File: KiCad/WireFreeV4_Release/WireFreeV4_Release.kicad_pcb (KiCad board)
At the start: 6 copper layers, 14.3 x 15.4 mm, 44 parts, among them J1 Conn_01x05, J10 Conn_01x01, J11 Conn_01x01, J12 Conn_01x01, J13 Conn_01x01, J14 Conn_01x01, J15 Conn_01x01, J2 Conn_01x28, J3 Conn_01x01, J4 Conn_01x01, J8 0475710001, U1 TPS62402-Q1, U2 MAX13030EETE+, U3 ATSAME70N21A-CN, U4 TSOP57438TT1, Y1 ABM8G-12.000MHZ-4Y-T3

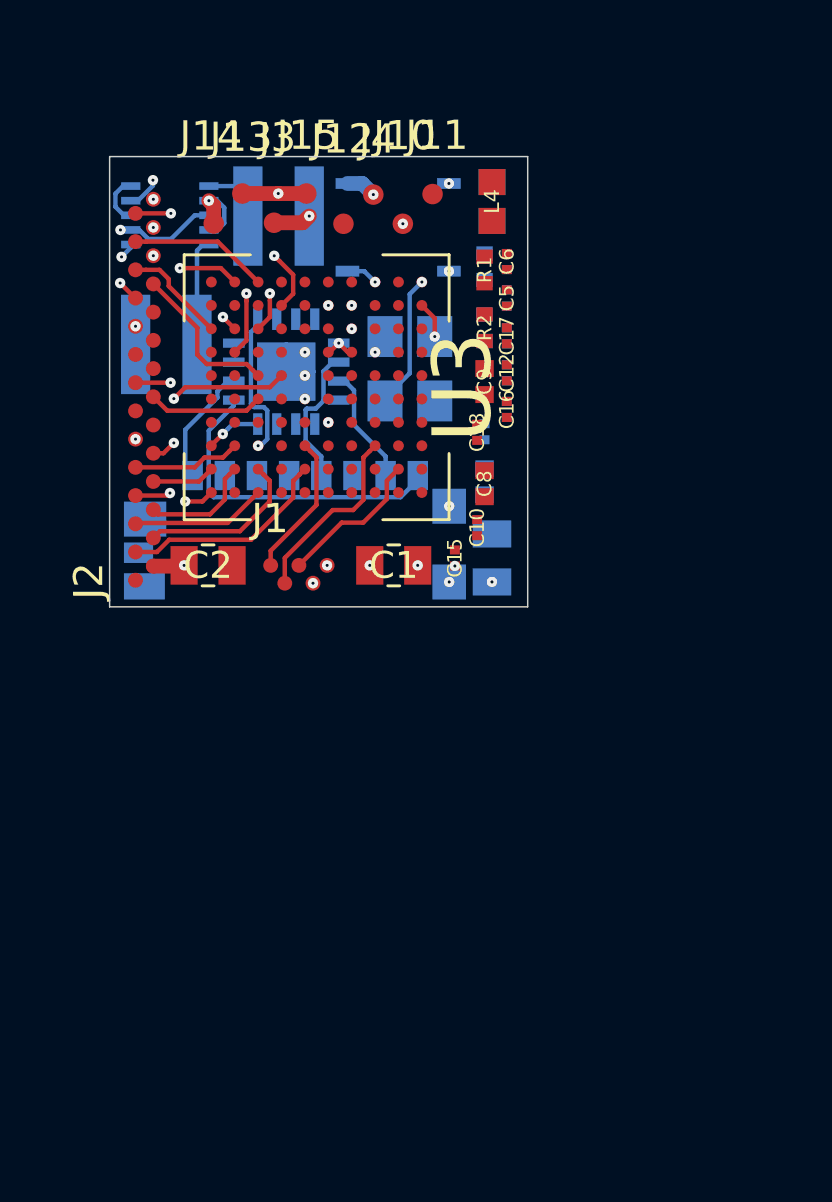
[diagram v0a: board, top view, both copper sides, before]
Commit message: Wire-free KiCAD Updates
1. Almost all lines are connected except some power lines and a few signal lines that lead to capacitors

2. About ten capacitors left to find their spot on the board

3. Rearranged the capacitor locations and connector pad locations to bring power converter SMDs closer to the IU.
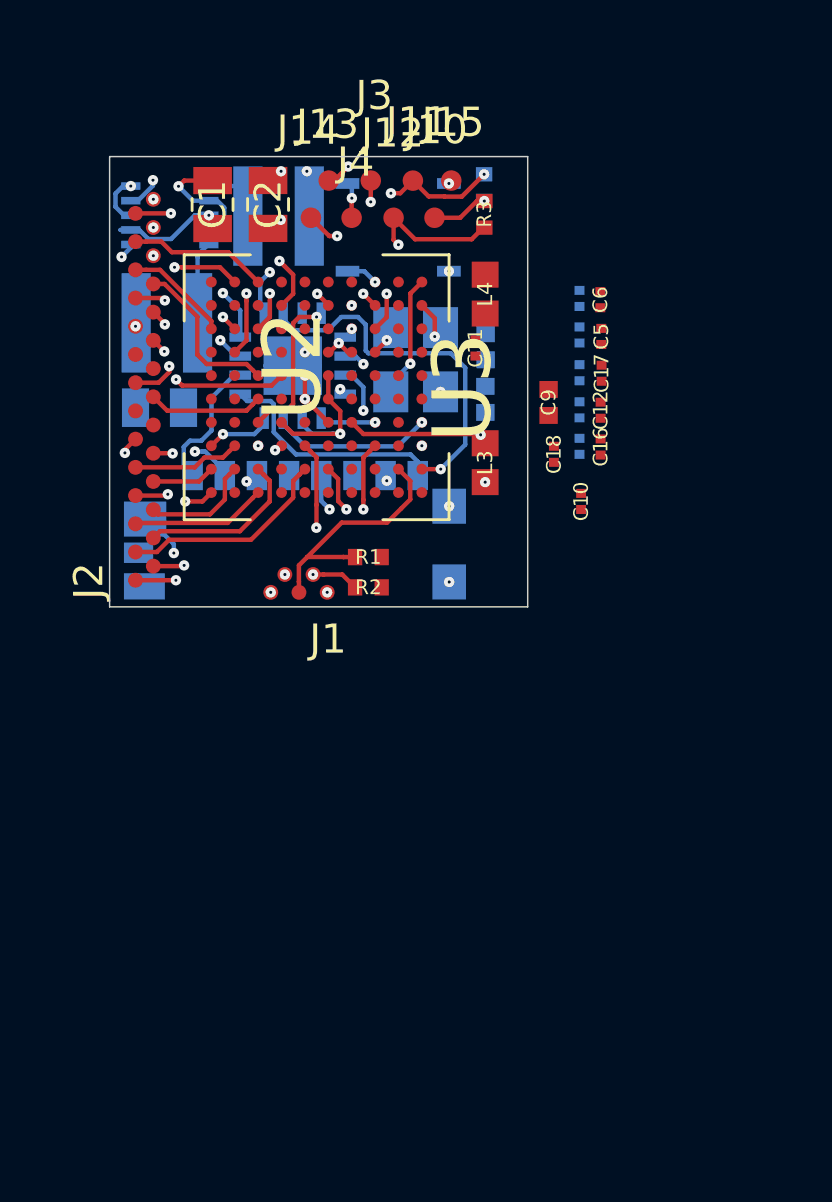
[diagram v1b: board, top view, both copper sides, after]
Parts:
- C11, L3, R3: moved to F.Cu
- C15, C8: moved to B.Cu
- moved C1 13.8 mm to (119.2, 72.2), turned to 270 degrees
- moved C2 12.5 mm to (121.1, 72.2), turned to 270 degrees
- moved C3 12.5 mm to (117.4, 79.2), turned to 0 degrees
- moved R1 10.6 mm to (124.6, 84.3), turned to 0 degrees
- moved R2 9.73 mm to (124.6, 85.3), turned to 0 degrees
- moved L3 8.94 mm to (128.5, 81.1), turned to 90 degrees
- moved J15 4.98 mm to (127.4, 71.4)
- moved C7 4.62 mm to (128.6, 77.1), turned to 270 degrees
- moved C15 4.03 mm to (128.4, 80.4)
- moved R3 3.88 mm to (128.5, 72.6)
- moved C10 3.67 mm to (131.8, 82.4)
- moved J3 3.61 mm to (124.6, 71.4)
- moved C5 3.49 mm to (132.5, 76.8)
- moved C17 3.49 mm to (132.5, 78.0)
- moved C16 3.46 mm to (132.5, 80.5)
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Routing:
- net /Connectors/SWDCLK: track 0.00 -> 16.6 mm, vias 0 -> 2
- net /Connectors/SWDIO: track 0.00 -> 14.6 mm, vias 0 -> 3
- net /MCU/SDCardCMDA: track 0.00 -> 12.5 mm, vias 0 -> 1
- net /SD Card/DAT3: track 0.00 -> 9.30 mm, vias 0 -> 2
- net Net-(J8-PadP3): track 0.00 -> 8.97 mm, vias 0 -> 2
- net +1V8: track 3.52 -> 11.4 mm, vias 4 -> 8
- net Earth: track 8.63 -> 14.8 mm, vias 17 -> 19
- net /MCU/SD1: track 0.00 -> 5.60 mm, vias 0 -> 1
- net /MCU/SDCardCLKA: track 0.00 -> 5.32 mm, vias 0 -> 1
- net /MCU/VDDPLL: track 0.00 -> 4.86 mm, vias 0 -> 1
- net /Connectors/SDA: track 5.14 -> 8.51 mm
- net /SD Card/DAT1: track 11.1 -> 8.06 mm
- net +BATT: track 4.36 -> 7.40 mm, vias 2 -> 4
- net /MCU/SD3: track 5.03 -> 7.97 mm, vias 1 -> 2
- net Net-(J8-PadP5): track 4.87 -> 7.45 mm, vias 0 -> 2
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
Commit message: Update Release Board KiCAD
1. Rotate the micro SD card mount
2. Place all capacitors
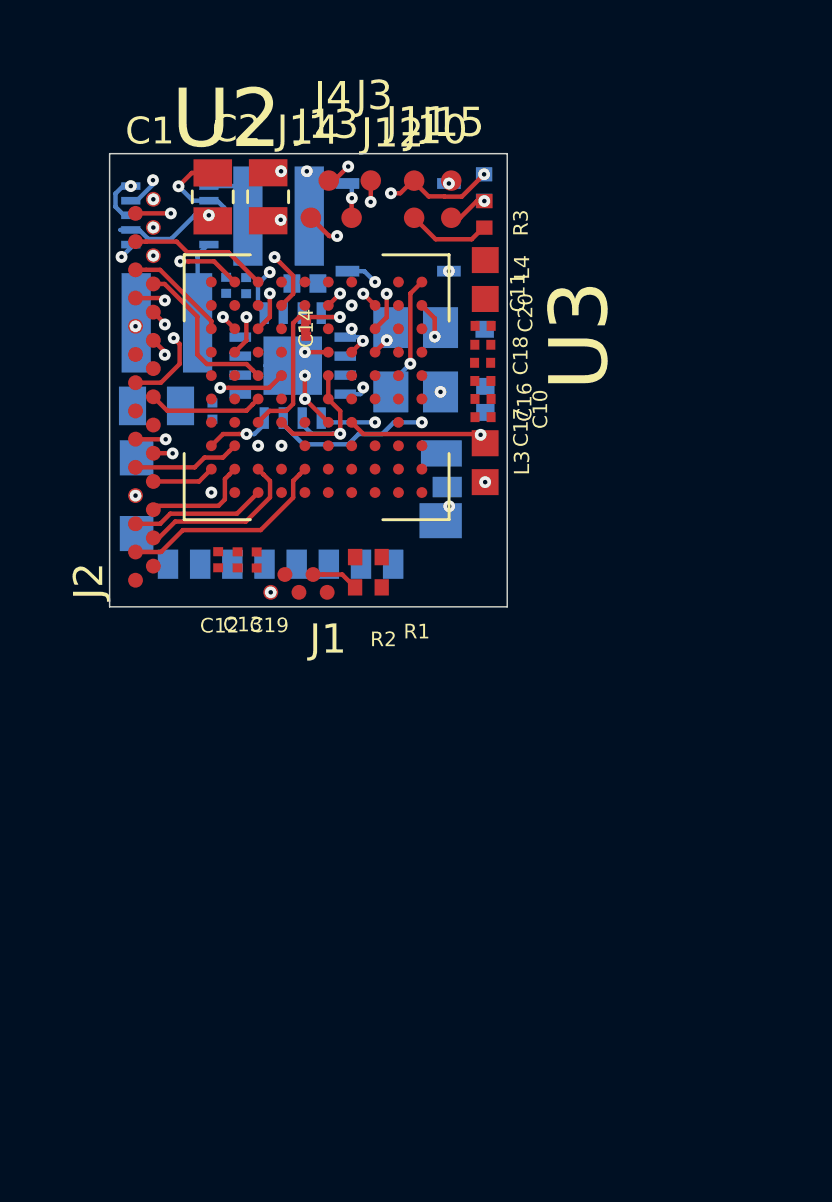
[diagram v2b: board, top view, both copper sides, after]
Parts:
- C13, C14, C19, C20: moved to F.Cu
- C5, C6, C9: moved to B.Cu
- moved C12 14.0 mm to (119.4, 84.4)
- moved C13 14.0 mm to (120.1, 84.4), turned to 90 degrees
- moved C6 13.8 mm to (119.2, 79.3)
- moved C5 13.0 mm to (119.7, 75.0), turned to 270 degrees
- moved C19 12.8 mm to (120.7, 84.4), turned to 90 degrees
- moved C4 11.4 mm to (120.4, 75.0)
- moved C14 9.76 mm to (122.4, 76.5), turned to 90 degrees
- moved C9 9.27 mm to (122.4, 74.9), turned to 180 degrees
- moved C16 4.96 mm to (128.5, 77.7), turned to 0 degrees
- moved C10 4.85 mm to (128.5, 78.9), turned to 180 degrees
- moved C18 4.47 mm to (128.5, 77.0), turned to 0 degrees
- moved C17 4.32 mm to (128.5, 79.5), turned to 180 degrees
- moved C20 3.99 mm to (128.5, 78.3), turned to 0 degrees
- moved J8 3.15 mm to (121.5, 84.5), turned to 0 degrees
- moved C7 1.04 mm to (128.5, 76.1), turned to 90 degrees
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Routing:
- net /Connectors/SWDCLK: track 16.6 -> 2.87 mm, vias 2 -> 0
- net /MCU/SDCardCMDA: track 12.5 -> 0.00 mm, vias 1 -> 0
- net /SD Card/DAT3: track 9.30 -> 0.00 mm, vias 2 -> 0
- net Net-(J8-PadP3): track 8.97 -> 0.00 mm, vias 2 -> 0
- net /Connectors/SDA: track 8.51 -> 0.00 mm
- net /SD Card/DAT1: track 8.06 -> 0.00 mm
- net Net-(J8-PadP5): track 7.45 -> 0.00 mm, vias 2 -> 0
- net /Connectors/LED_ENT: track 6.10 -> 0.00 mm, vias 2 -> 0
- net /Connectors/SCL: track 7.13 -> 1.62 mm, vias 2 -> 0
- net /SD Card/DAT2: track 5.14 -> 0.00 mm
- net /SD Card/DAT0: track 4.52 -> 0.00 mm, vias 2 -> 0
- net Earth: track 14.8 -> 12.7 mm, vias 19 -> 14
- net /CMOS Imaging Sensor Connectors/CLK_OUT: track 10.3 -> 8.55 mm
- net +1V8: track 11.4 -> 9.78 mm, vias 8 -> 7
- net /MCU/SDCardCLKA: track 5.32 -> 6.61 mm
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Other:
- board size 14.3 x 15.4 mm -> 13.6 x 15.5 mm

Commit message: Update WireFreeV4_Release.kicad_pcb
Last update before an overhaul:

1. Change SWD to Pogo pins
2. Rearrange the capacitors and pins
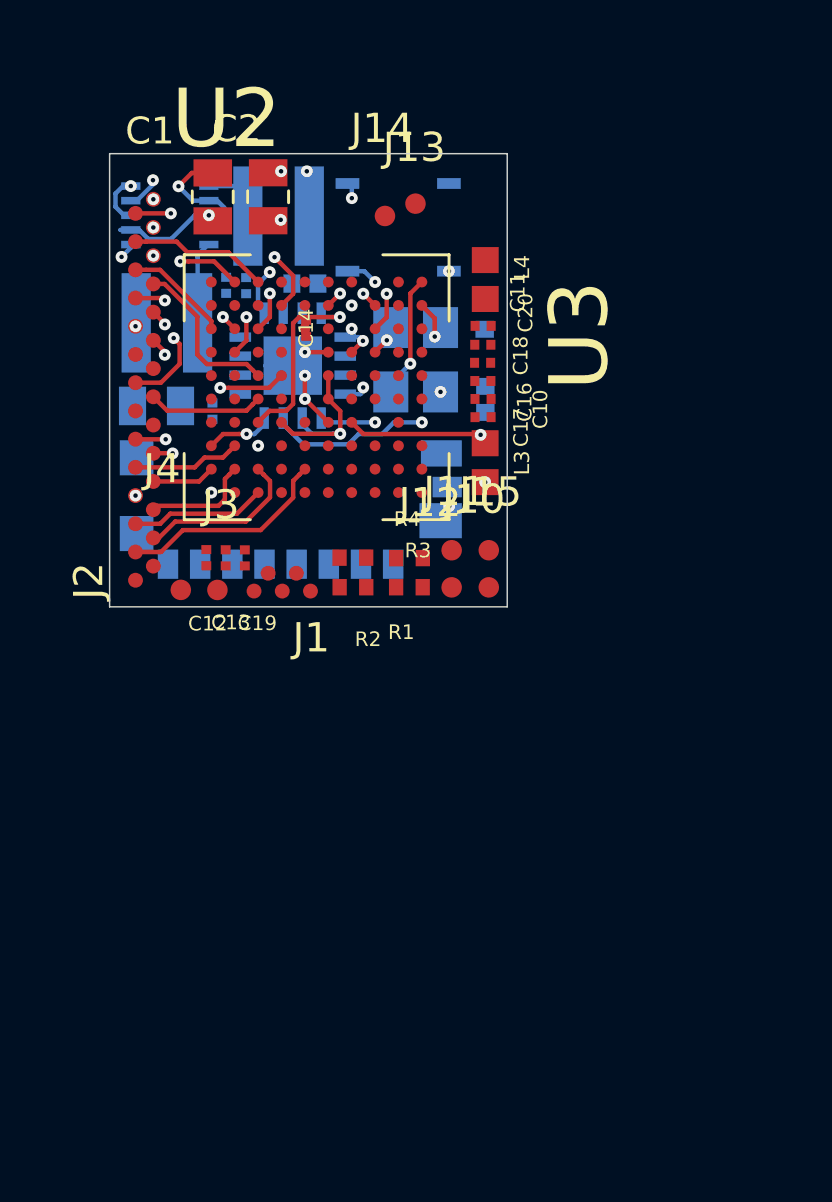
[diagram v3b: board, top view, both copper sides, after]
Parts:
- R4: moved to F.Cu
- moved J3 15.0 mm to (119.4, 85.4)
- moved J4 14.0 mm to (118.1, 85.4)
- moved R3 13.0 mm to (126.0, 85.3), turned to 0 degrees
- moved R4 12.9 mm to (126.0, 84.3), turned to 0 degrees
- moved J12 12.7 mm to (126.7, 85.3)
- moved J11 12.7 mm to (127.4, 84.1)
- moved J15 12.7 mm to (128.7, 84.1)
- moved J10 12.7 mm to (128.1, 85.3)
- moved J13 3.07 mm to (126.2, 72.2)
- moved J14 2.53 mm to (125.1, 72.6)
- moved J1 0.57 mm to (122.6, 85.5)
- moved R1 0.53 mm to (124.0, 84.3)
- moved R2 0.53 mm to (124.0, 85.3)
- moved C19 0.41 mm to (120.3, 84.3)
- moved C12 0.41 mm to (119.0, 84.3)
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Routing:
- net /Connectors/SWDIO: track 14.1 -> 0.00 mm, vias 3 -> 0
- net /Connectors/SWDCLK: track 2.87 -> 0.00 mm
- net +1V8: track 9.78 -> 7.68 mm, vias 7 -> 5
- net /Connectors/SCL: track 1.62 -> 0.00 mm
- net +BATT: track 7.63 -> 6.48 mm, vias 4 -> 3
- net Earth: track 12.7 -> 11.9 mm, vias 14 -> 12
- net +3V3: track 2.58 -> 1.92 mm, vias 5 -> 4

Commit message: PCB Layout Overhaul
1. Places the microSD and MCU on the same side

2. Sketches the outline with the components placed

3. No traces or vias yet
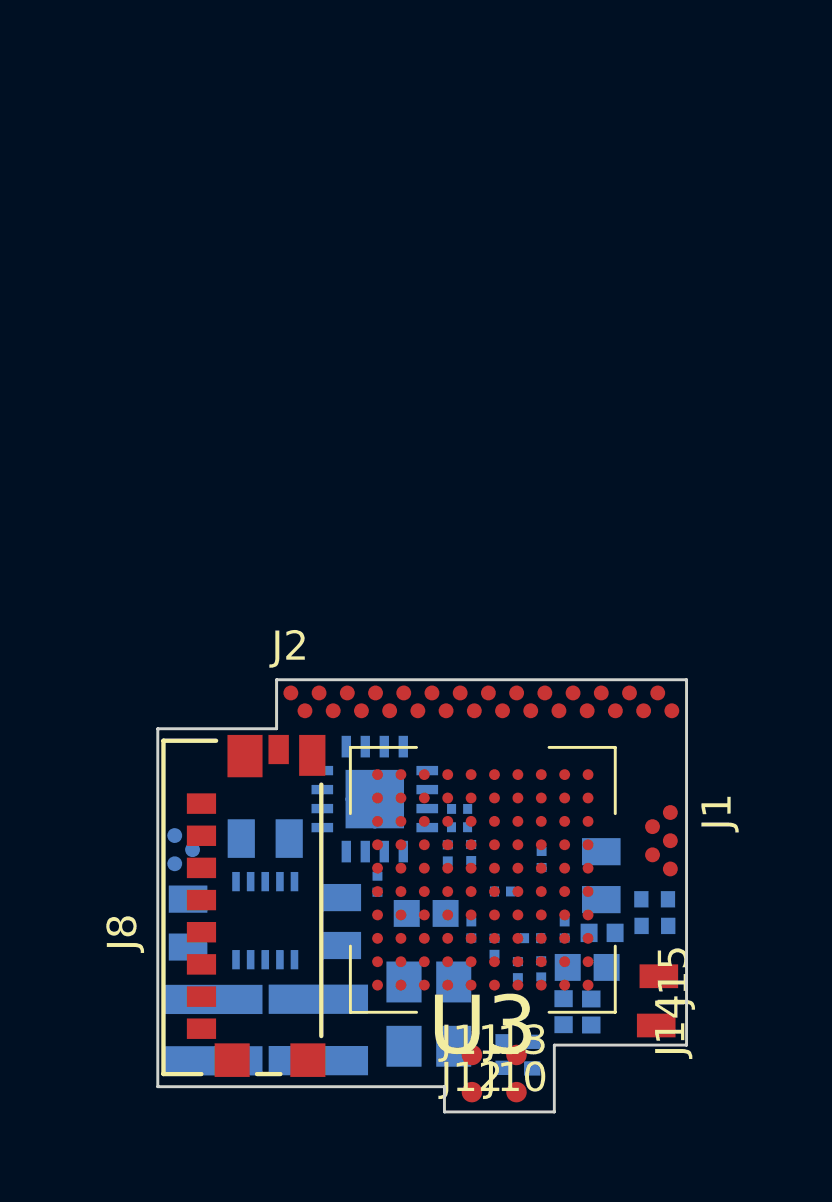
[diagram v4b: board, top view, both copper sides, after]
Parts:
- removed J4: Conn_01x01, .Connector:Conn_1x1_700_Circular_Pad
- removed U4: TSOP57438TT1, .Package_SON:SON_4_P300_395X395X90L55X35L
- added C21: C_Small, .Capacitor:C_0805_2012Metric_L, B.Cu at (132.5, 95.2)
- C1, C10, C11, C12, C13, C14, C16, C17, C18, C19, C2, C20, L3, L4, R1, R2, R3, R4: moved to B.Cu
- J14, J15: footprint .Connector:Conn_1x1_700_Circular_Pad -> .Connector:Conn_1x1_250x750_Pad
- J3: value Conn_01x01 -> Conn_01x03; footprint .Connector:Conn_1x1_700_Circular_Pad -> .Connector:B2B_Flex_03_Dual_Row_38milx24mil_Pad_20mil_copy; moved to B.Cu
- J8: moved to F.Cu
- moved J13 29.3 mm to (129.6, 101.3), turned to 180 degrees
- moved J14 29.2 mm to (134.4, 100.3), turned to 90 degrees
- moved L1 27.9 mm to (119.2, 100.5), turned to 270 degrees
- moved C2 25.0 mm to (118.4, 96.8), turned to 90 degrees
- moved L2 24.7 mm to (122.8, 100.5), turned to 270 degrees
- moved C9 24.4 mm to (132.5, 97.2), turned to 0 degrees
- moved U1 24.3 mm to (121.0, 96.7), turned to 180 degrees
- moved C7 23.9 mm to (131.2, 99.8), turned to 270 degrees
- moved L4 23.8 mm to (132.0, 98.3), turned to 0 degrees
- moved Y1 22.4 mm to (126.6, 99.9), turned to 270 degrees
- moved C11 22.1 mm to (130.5, 98.4), turned to 270 degrees
- moved C1 22.0 mm to (121.0, 93.9), turned to 0 degrees
- moved C18 21.4 mm to (129.7, 98.4), turned to 270 degrees
- moved C8 21.3 mm to (132.2, 99.9)
- moved C4 21.0 mm to (124.9, 95.5)
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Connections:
- J3 pad 1: +1V8 -> Earth
- U3 pad C1: /MCU/IR_Receiver -> /Connectors/IR_Receiver
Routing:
- net Earth: track 11.9 -> 0.00 mm, vias 12 -> 0
- net /CMOS Imaging Sensor Connectors/CLK_OUT: track 8.55 -> 0.00 mm, vias 2 -> 0
- net /MCU/SD3: track 8.12 -> 0.00 mm, vias 2 -> 0
- net /CMOS Imaging Sensor Connectors/RESET_N: track 7.90 -> 0.00 mm, vias 2 -> 0
- net +1V8: track 7.68 -> 0.00 mm, vias 5 -> 0
- net /CMOS Imaging Sensor Connectors/LINE_VALID: track 7.62 -> 0.00 mm, vias 2 -> 0
- net /CMOS Imaging Sensor Connectors/Status_LED: track 7.50 -> 0.00 mm, vias 2 -> 0
- net /CMOS Imaging Sensor Connectors/img_d0: track 7.30 -> 0.00 mm
- net /CMOS Imaging Sensor Connectors/SCK: track 7.19 -> 0.00 mm, vias 2 -> 0
- net /CMOS Imaging Sensor Connectors/SS_N: track 6.69 -> 0.00 mm, vias 2 -> 0
- net /MCU/SDCardCLKA: track 6.61 -> 0.00 mm, vias 1 -> 0
- net +BATT: track 6.48 -> 0.00 mm, vias 3 -> 0
- net /CMOS Imaging Sensor Connectors/MONITOR0: track 6.46 -> 0.00 mm, vias 2 -> 0
- net /CMOS Imaging Sensor Connectors/img_d7: track 5.85 -> 0.00 mm, vias 2 -> 0
- net /CMOS Imaging Sensor Connectors/img_d2: track 5.70 -> 0.00 mm
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- removed copper zone on In1.Cu, net Earth
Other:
- board size 13.6 x 15.5 mm -> 18.1 x 14.8 mm

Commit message: Rearrange Release Board
1. 28-flexPC pad changed to 25-pads by eliminating the vBatt, and the I2C's

2. Dimensions: 18.92mm x 12.09mm
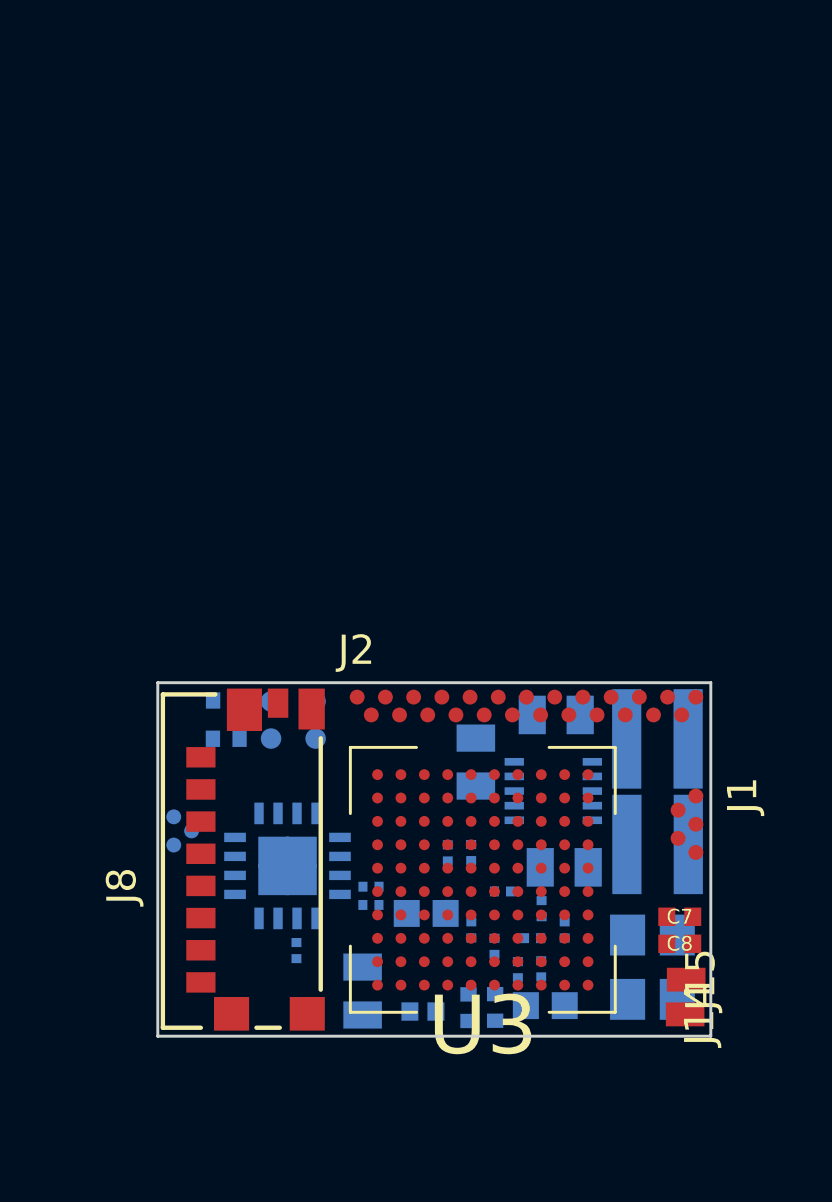
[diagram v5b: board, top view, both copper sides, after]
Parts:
- C7, C8: moved to F.Cu
- J10, J11, J12, J13: moved to B.Cu
- J2: value Conn_01x28 -> Conn_01x25; footprint .Connector:B2B_Flex_28_Dual_Row_38milx24mil_Pad_20mil -> .Connector:B2B_Flex_25_Dual_Row_38milx24mil_Pad_20mil
- moved L1 16.5 mm to (134.4, 94.1), turned to 0 degrees
- moved R3 16.0 mm to (119.7, 89.2), turned to 0 degrees
- moved L2 15.3 mm to (134.4, 90.5), turned to 0 degrees
- moved J10 15.0 mm to (122.7, 89.2)
- moved J12 15.0 mm to (121.2, 89.2)
- moved R4 14.4 mm to (119.7, 90.5), turned to 0 degrees
- moved C2 13.0 mm to (131.2, 94.9), turned to 180 degrees
- moved J11 12.8 mm to (121.2, 90.5)
- moved J13 12.8 mm to (122.7, 90.5)
- moved U1 10.8 mm to (130.9, 92.3), turned to 270 degrees
- moved C3 10.2 mm to (131.0, 89.7), turned to 180 degrees
- moved C21 9.07 mm to (124.4, 99.1), turned to 270 degrees
- moved Y1 7.81 mm to (134.3, 98.3), turned to 90 degrees
- moved C1 7.66 mm to (128.2, 91.3), turned to 90 degrees
- moved R1 6.96 mm to (128.0, 99.7), turned to 270 degrees
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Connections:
- net /Connectors/IR_Receiver renamed /External Connectors/IR_Receiver
- net /Connectors/LED_ENT renamed /External Connectors/LED_ENT
- net /Connectors/SCL renamed /External Connectors/SCL
- net /Connectors/SDA renamed /External Connectors/SDA
- net /Connectors/SWDCLK renamed /External Connectors/SWDCLK
- net /Connectors/SWDIO renamed /External Connectors/SWDIO
- J2 pad 16: /CMOS Imaging Sensor Connectors/I2C_SDA1 -> +3V3
- J2 pad 17: /CMOS Imaging Sensor Connectors/I2C_SCL1 -> Earth
- J2 pad 18: +BATT -> /CMOS Imaging Sensor Connectors/Status_LED
- J2 pad 19: +3V3 -> /CMOS Imaging Sensor Connectors/MOSI
- J2 pad 20: Earth -> /CMOS Imaging Sensor Connectors/MISO
- J2 pad 21: /CMOS Imaging Sensor Connectors/Status_LED -> /CMOS Imaging Sensor Connectors/MONITOR0
- J2 pad 22: /CMOS Imaging Sensor Connectors/MOSI -> /CMOS Imaging Sensor Connectors/TRIGGER0
- J2 pad 23: /CMOS Imaging Sensor Connectors/MISO -> /CMOS Imaging Sensor Connectors/RESET_N
- J2 pad 24: /CMOS Imaging Sensor Connectors/MONITOR0 -> /CMOS Imaging Sensor Connectors/SCK
- J2 pad 25: /CMOS Imaging Sensor Connectors/TRIGGER0 -> /CMOS Imaging Sensor Connectors/SS_N
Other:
- board size 18.1 x 14.8 mm -> 18.9 x 12.1 mm
